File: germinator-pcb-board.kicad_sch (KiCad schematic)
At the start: 10 parts, among them J1 Conn_01x15_Socket, J2 Conn_01x15_Socket, J3 Screw_Terminal_01x04, J4 Screw_Terminal_01x03, J5 Screw_Terminal_01x03, J6 Screw_Terminal_01x03, J7 Screw_Terminal_01x03, U1 ESP32-DEVKIT-V1

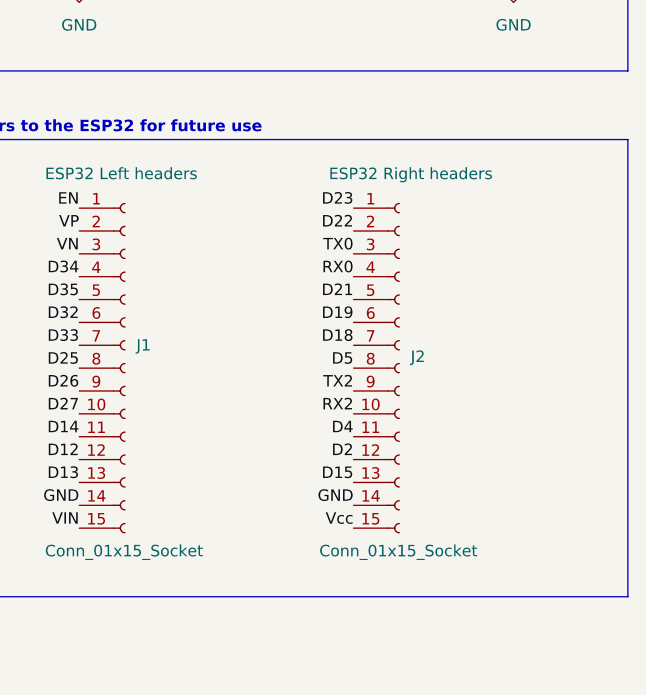
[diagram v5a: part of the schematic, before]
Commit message: Layout Step 2: Outline and Mechanical Constraints
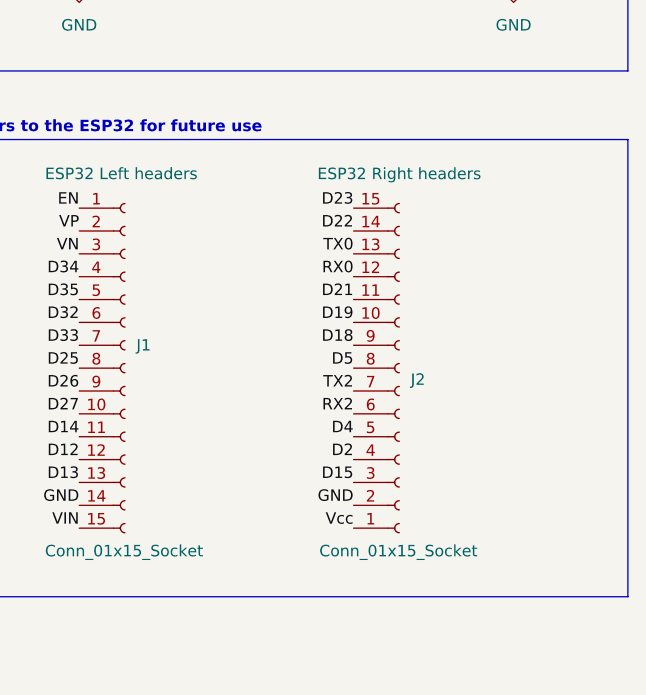
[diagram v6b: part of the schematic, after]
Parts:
- J1, J2: footprint (none) -> Connector_PinSocket_2.54mm:PinSocket_1x15_P2.54mm_Vertical
- U1: footprint ESP32-DEVKIT-V1:MODULE_ESP32_DEVKIT_V1 -> germinator-pcb-board-libraries:ESP32_DEVKIT_V1; Availability Not in stock -> (none); Check_prices https://www.snapeda.com/parts/ESP32-DEVKIT-V1/Do+it/view-pa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 -> (none); Description_1 Dual core, Wi-Fi: 2.4 GHz up to 150 Mbits/s,BLE (Bluetooth 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 -> (none); MANUFACTURER DOIT -> (none); MAXIMUM_PACKAGE_HEIGHT 6.8 mm -> (none); MF Do it -> (none); MP ESP32-DEVKIT-V1 -> (none); PARTREV N/A -> (none); Package None -> (none); Price None -> (none); STANDARD Manufacturer Recommendations -> (none); SnapEDA_Link https://www.snapeda.com/parts/ESP32-DEVKIT-V1/Do+it/view-pa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 -> (none)
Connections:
- net D15: now also J2.3 (Pin_3); no longer J2.13 (Pin_13)
- net D18: now also J2.9 (Pin_9); no longer J2.7 (Pin_7)
- net D19: now also J2.10 (Pin_10); no longer J2.6 (Pin_6)
- net D2: now also J2.4 (Pin_4); no longer J2.12 (Pin_12)
- net D21: now also J2.11 (Pin_11); no longer J2.5 (Pin_5)
- net D22: now also J2.14 (Pin_14); no longer J2.2 (Pin_2)
- net D23: now also J2.15 (Pin_15); no longer J2.1 (Pin_1)
- net D4: now also J2.5 (Pin_5); no longer J2.11 (Pin_11)
- net GND: now also J2.2 (Pin_2); no longer J2.14 (Pin_14)
- net RX0: now also J2.12 (Pin_12); no longer J2.4 (Pin_4)
- net RX2: now also J2.6 (Pin_6); no longer J2.10 (Pin_10)
- net TX0: now also J2.13 (Pin_13); no longer J2.3 (Pin_3)
- net TX2: now also J2.7 (Pin_7); no longer J2.9 (Pin_9)
- net Vcc: now also J2.1 (Pin_1); no longer J2.15 (Pin_15)
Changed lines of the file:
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@@
 			)
 		)
-		(property "Footprint" ""
+		(property "Footprint" "Connector_PinSocket_2.54mm:PinSocket_1x15_P2.54mm_Vertical"
 			(at 198.12 134.62 0)
 			(effects
@@
 		(lib_id "Connector:Conn_01x15_Socket")
 		(at 228.6 134.62 0)
+		(mirror x)
 		(unit 1)
 		(exclude_from_sim no)
@@
 		(dnp no)
 		(property "Reference" "J2"
-			(at 229.87 133.3499 0)
+			(at 229.87 135.8901 0)
 			(effects
 				(font
@@
 			)
 		)
-		(property "Footprint" ""
+		(property "Footprint" "Connector_PinSocket_2.54mm:PinSocket_1x15_P2.54mm_Vertical"
 			(at 228.6 134.62 0)
 			(effects
@@
 		)
 		(property "Purpose" "ESP32 Right headers"
-			(at 229.87 113.03 0)
+			(at 228.6 113.03 0)
 			(effects
 				(font
@@
 			)
 		)
-		(property "Footprint" "ESP32-DEVKIT-V1:MODULE_ESP32_DEVKIT_V1"
+		(property "Footprint" "germinator-pcb-board-libraries:ESP32_DEVKIT_V1"
 			(at 218.44 63.5 0)
 			(effects
@@
 			)
 		)
-		(property "MANUFACTURER" "DOIT"
-			(at 218.44 63.5 0)
-			(effects
-				(font
-					(size 1.27 1.27)
-				)
-				(justify bottom)
-				(hide yes)
-			)
-		)
 		(property "Purpose" "ESP32 Controller"
 			(at 218.44 92.71 0)
@@
 			)
 		)
-		(property "MF" "Do it"
-			(at 218.44 63.5 0)
-			(effects
-				(font
-					(size 1.27 1.27)
-				)
-				(justify bottom)
-				(hide yes)
-			)
-		)
-		(property "MAXIMUM_PACKAGE_HEIGHT" "6.8 mm"
-			(at 218.44 63.5 0)
-			(effects
-				(font
-					(size 1.27 1.27)
-				)
-				(justify bottom)
-				(hide yes)
-			)
-		)
-		(property "Package" "None"
-			(at 218.44 63.5 0)
-			(effects
-				(font
-					(size 1.27 1.27)
-				)
-				(justify bottom)
-				(hide yes)
-			)
-		)
-		(property "Price" "None"
-			(at 218.44 63.5 0)
-			(effects
-				(font
-					(size 1.27 1.27)
-				)
-				(justify bottom)
-				(hide yes)
-			)
-		)
-		(property "Check_prices" "https://www.snapeda.com/parts/ESP32-DEVKIT-V1/Do+it/view-part/?ref=eda"
-			(at 218.44 63.5 0)
-			(effects
-				(font
-					(size 1.27 1.27)
-				)
-				(justify bottom)
-				(hide yes)
-			)
-		)
-		(property "STANDARD" "Manufacturer Recommendations"
-			(at 218.44 63.5 0)
-			(effects
-				(font
-					(size 1.27 1.27)
-				)
-				(justify bottom)
-				(hide yes)
-			)
-		)
-		(property "PARTREV" "N/A"
-			(at 218.44 63.5 0)
-			(effects
-				(font
-					(size 1.27 1.27)
-				)
-				(justify bottom)
-				(hide yes)
-			)
-		)
-		(property "SnapEDA_Link" "https://www.snapeda.com/parts/ESP32-DEVKIT-V1/Do+it/view-part/?ref=snap"
-			(at 218.44 63.5 0)
-			(effects
-				(font
-					(size 1.27 1.27)
-				)
-				(justify bottom)
-				(hide yes)
-			)
-		)
-		(property "MP" "ESP32-DEVKIT-V1"
-			(at 218.44 63.5 0)
-			(effects
-				(font
-					(size 1.27 1.27)
-				)
-				(justify bottom)
-				(hide yes)
-			)
-		)
-		(property "Description_1" "\n                        \n                            Dual core, Wi-Fi: 2.4 GHz up to 150 Mbits/s,BLE (Bluetooth Low Energy) and legacy Bluetooth, 32 bits, Up to 240 MHz\n                        \n"
-			(at 218.44 63.5 0)
-			(effects
-				(font
-					(size 1.27 1.27)
-				)
-				(justify bottom)
-				(hide yes)
-			)
-		)
-		(property "Availability" "Not in stock"
-			(at 218.44 63.5 0)
-			(effects
-				(font
-					(size 1.27 1.27)
-				)
-				(justify bottom)
-				(hide yes)
-			)
-		)
